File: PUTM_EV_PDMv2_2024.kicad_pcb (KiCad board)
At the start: 4 copper layers, 58 x 87.3 mm, 138 parts, among them IC1 BTS722204ESAXUMA1, IC2 BTS722204ESAXUMA1, IC3 BTS722204ESAXUMA1, IC4 BTS722204ESAXUMA1, J1 74650073R, J4 Conn_01x06, J5 UMPT-08-01-L-RA-WT-P-TR, J6 FTSH-107-01-L-DV-K-A, J7 USB_C_Receptacle_USB2.0_14P, J8 UMPT-08-01-L-RA-WT-P-TR, U1 STM32G0C1KCTxN, U2 LD1117S33TR_SOT223, U3 LM2675M-5.0/NOPB, U4 MCP2542FDxMF

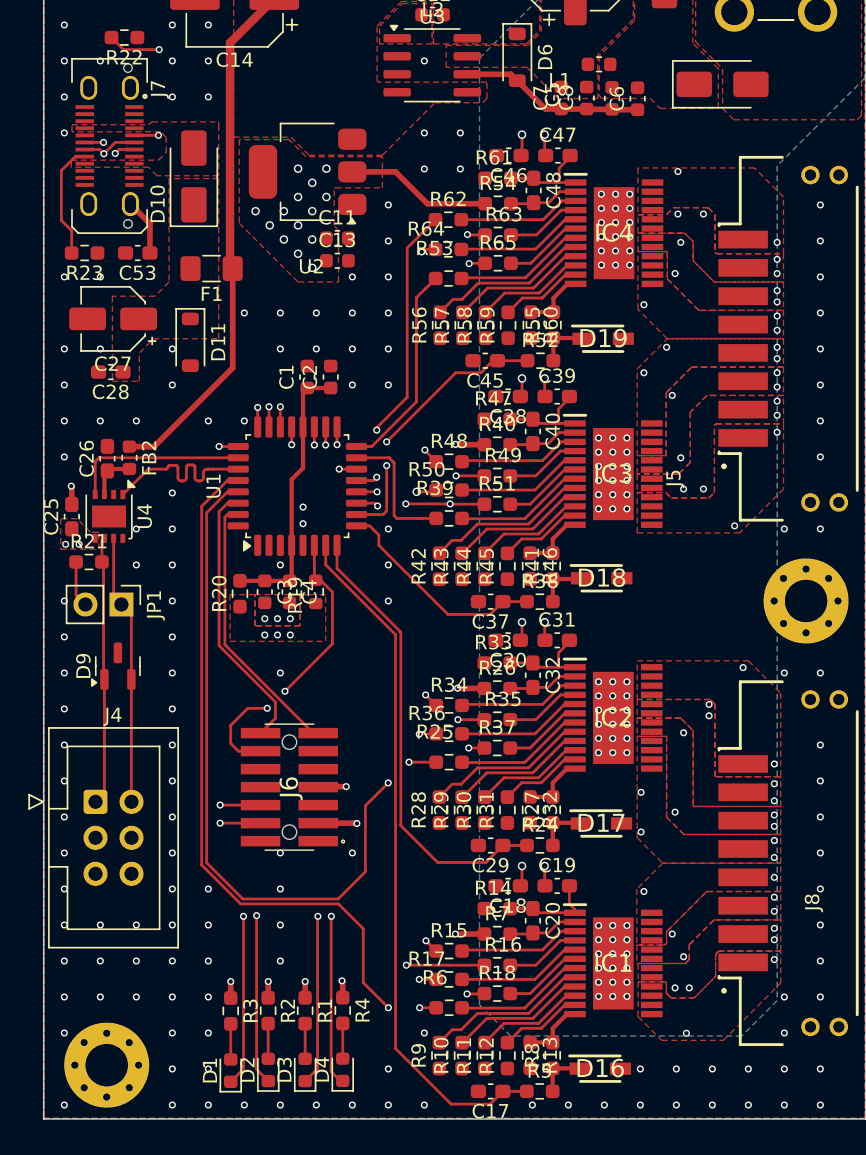
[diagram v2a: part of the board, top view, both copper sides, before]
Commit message: Minor changes
Added battery zone on the f.cu
Easier connector soldering (additional pads)
Changed 3.3V layer
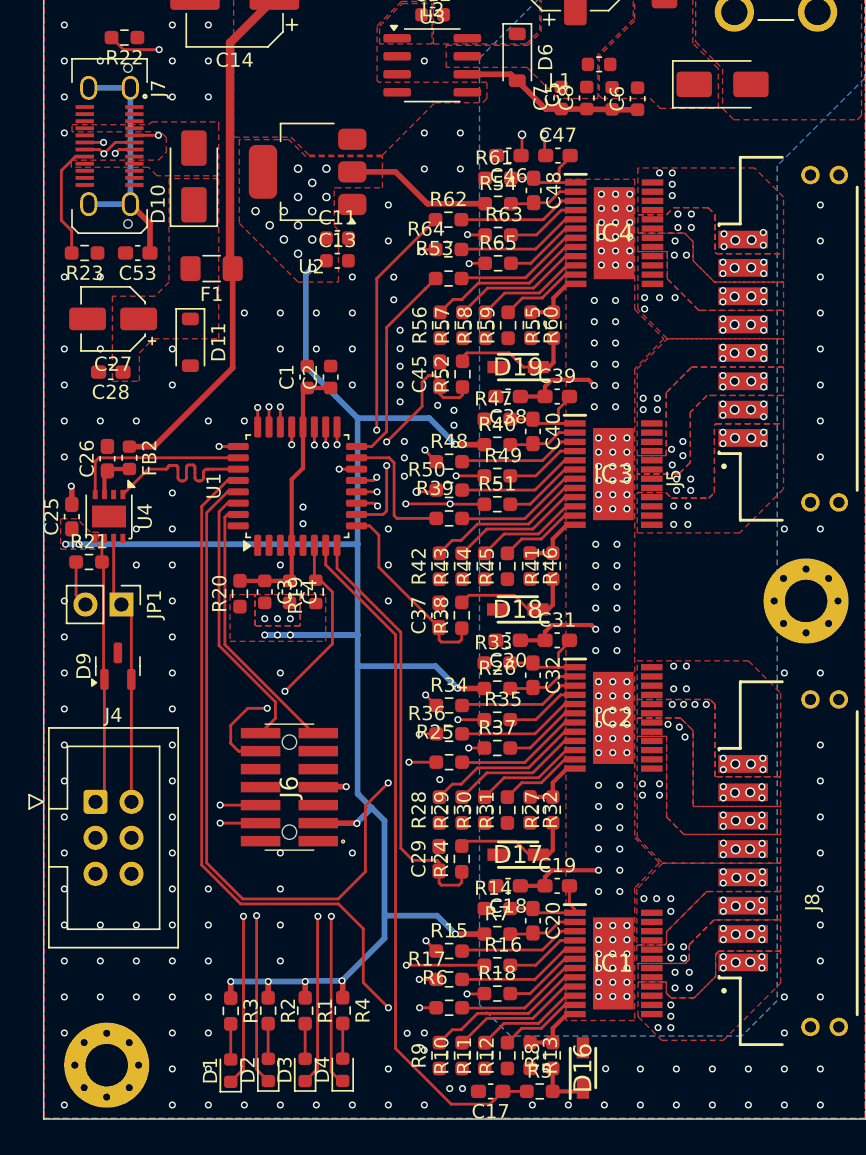
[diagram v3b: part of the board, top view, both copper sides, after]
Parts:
- moved D19 6.32 mm to (154.3, 88.8), turned to 180 degrees
- moved D18 6.32 mm to (154.2, 105.8), turned to 180 degrees
- moved D17 6.27 mm to (154.3, 123.2), turned to 180 degrees
- moved R38 5.60 mm to (150.3, 106.3), turned to 90 degrees
- moved R24 5.59 mm to (150.3, 123.5), turned to 90 degrees
- moved R52 5.58 mm to (150.3, 89.2), turned to 90 degrees
- moved C37 3.76 mm to (148.7, 106.3), turned to 90 degrees
- moved C29 3.76 mm to (148.7, 123.4), turned to 90 degrees
- moved C45 3.35 mm to (148.8, 89.2), turned to 90 degrees
- moved D16 1.23 mm to (158.8, 138.2), turned to 90 degrees
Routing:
- net +BATT: track 11.1 -> 21.9 mm, vias 80 -> 110
- net Net-(D19-K): track 3.70 -> 9.11 mm
- net Net-(D17-K): track 3.63 -> 9.02 mm
- net Net-(D18-K): track 3.65 -> 9.00 mm
- net /FUSE4_IS: track 19.4 -> 17.2 mm
- net /FUSE3_IS: track 15.4 -> 13.5 mm
- net /FUSE2_IS: track 32.1 -> 30.3 mm
- net OUT4_3: vias 3 -> 10
- net OUT4_2: vias 4 -> 9
- net OUT4_1: vias 4 -> 10
- net OUT4_0: vias 2 -> 10
- net OUT3_3: vias 2 -> 10
- net OUT3_2: vias 4 -> 10
- net OUT3_1: vias 4 -> 10
- net OUT3_0: vias 4 -> 10
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- added copper zone on B.Cu, net OUT1_0
- added copper zone on B.Cu, net OUT1_1
- added copper zone on B.Cu, net OUT1_2
- added copper zone on B.Cu, net OUT1_3
- added copper zone on B.Cu, net OUT2_0
- added copper zone on B.Cu, net OUT2_1
- added copper zone on B.Cu, net OUT2_2
- added copper zone on B.Cu, net OUT2_3
- added copper zone on B.Cu, net OUT3_0
- added copper zone on B.Cu, net OUT3_1
- added copper zone on B.Cu, net OUT3_2
- added copper zone on B.Cu, net OUT3_3
- added copper zone on B.Cu, net OUT4_0
- added copper zone on B.Cu, net OUT4_1
- added copper zone on B.Cu, net OUT4_2
- added copper zone on B.Cu, net OUT4_3

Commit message: Production
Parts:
- added C21: 10n, Capacitor_SMD:C_0603_1608Metric_Pad1.08x0.95mm_HandSolder, B.Cu at (173.2, 124.8)
- added C22: 10n, Capacitor_SMD:C_0603_1608Metric_Pad1.08x0.95mm_HandSolder, B.Cu at (173.2, 126.8)
- added C23: 10n, Capacitor_SMD:C_0603_1608Metric_Pad1.08x0.95mm_HandSolder, B.Cu at (173.2, 128.8)
- added C24: 10n, Capacitor_SMD:C_0603_1608Metric_Pad1.08x0.95mm_HandSolder, B.Cu at (173.2, 130.8)
- added C33: 10n, Capacitor_SMD:C_0603_1608Metric_Pad1.08x0.95mm_HandSolder, B.Cu at (173.2, 116.8)
- added C34: 10n, Capacitor_SMD:C_0603_1608Metric_Pad1.08x0.95mm_HandSolder, B.Cu at (173.2, 118.8)
- added C35: 10n, Capacitor_SMD:C_0603_1608Metric_Pad1.08x0.95mm_HandSolder, B.Cu at (173.2, 120.8)
- added C36: 10n, Capacitor_SMD:C_0603_1608Metric_Pad1.08x0.95mm_HandSolder, B.Cu at (173.2, 122.8)
- added C41: 10n, Capacitor_SMD:C_0603_1608Metric_Pad1.08x0.95mm_HandSolder, B.Cu at (173.3, 87.7)
- added C42: 10n, Capacitor_SMD:C_0603_1608Metric_Pad1.08x0.95mm_HandSolder, B.Cu at (173.3, 89.7)
- added C43: 10n, Capacitor_SMD:C_0603_1608Metric_Pad1.08x0.95mm_HandSolder, B.Cu at (173.3, 91.8)
- added C44: 10n, Capacitor_SMD:C_0603_1608Metric_Pad1.08x0.95mm_HandSolder, B.Cu at (173.2, 93.8)
- added C49: 10n, Capacitor_SMD:C_0603_1608Metric_Pad1.08x0.95mm_HandSolder, B.Cu at (173.3, 79.8)
- added C50: 10n, Capacitor_SMD:C_0603_1608Metric_Pad1.08x0.95mm_HandSolder, B.Cu at (173.3, 81.8)
- added C51: 10n, Capacitor_SMD:C_0603_1608Metric_Pad1.08x0.95mm_HandSolder, B.Cu at (173.3, 83.8)
- added C52: 10n, Capacitor_SMD:C_0603_1608Metric_Pad1.08x0.95mm_HandSolder, B.Cu at (173.3, 85.8)
- added G***: LOGO, LOGO, F.Cu at (127.5, 88.3)
- added G***: LOGO, LOGO, B.Cu at (165.8, 104.8)
- added G***: LOGO, Logos:SignatureBox25mm, B.Cu at (153.7, 60.6)
- added G***: LOGO, LOGO, B.Cu at (175.5, 139.0)
- added G***: LOGO, logos:PUTM_LOGO_15mm, B.Cu at (135.7, 58.3)
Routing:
- net OUT4_0: track 0.00 -> 1.09 mm
- net OUT2_1: track 0.00 -> 1.07 mm
- net OUT2_2: track 0.00 -> 1.04 mm
- net OUT2_3: track 0.00 -> 1.03 mm
- net OUT1_3: track 0.00 -> 1.03 mm
- net OUT4_3: track 0.00 -> 1.02 mm
- net OUT4_2: track 0.00 -> 1.02 mm
- net OUT4_1: track 0.00 -> 1.02 mm
- net OUT1_2: track 0.00 -> 0.99 mm
- net OUT1_1: track 0.00 -> 0.99 mm
- net OUT3_2: track 0.00 -> 0.98 mm
- net OUT2_0: track 0.00 -> 0.97 mm
- net OUT3_1: track 0.00 -> 0.96 mm
- net OUT3_0: track 0.00 -> 0.96 mm
- net OUT3_3: track 0.00 -> 0.95 mm
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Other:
- board text added: "Kacper Biadała"
- board text added: "v2.0"

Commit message: Production
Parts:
- removed the G*** at (127.5, 88.3)

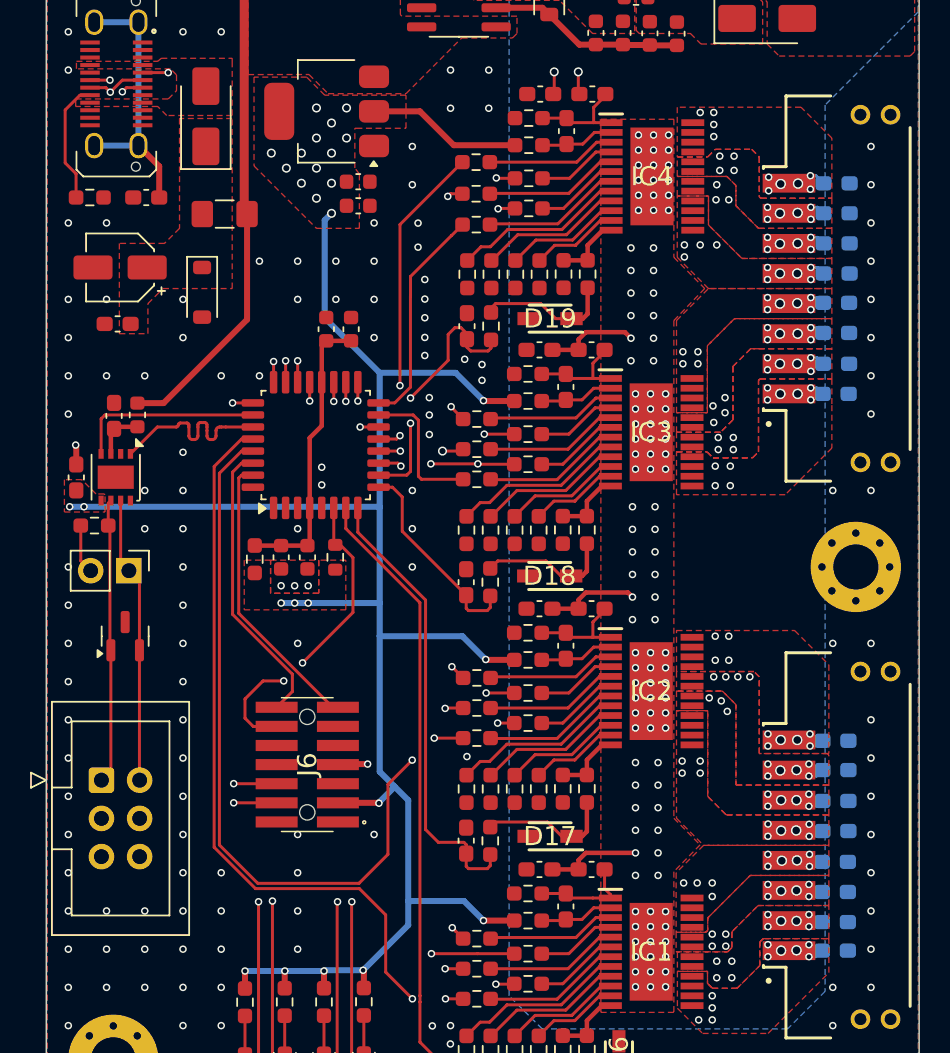
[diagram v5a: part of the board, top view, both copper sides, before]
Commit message: Minor fixes
added USBc tvs
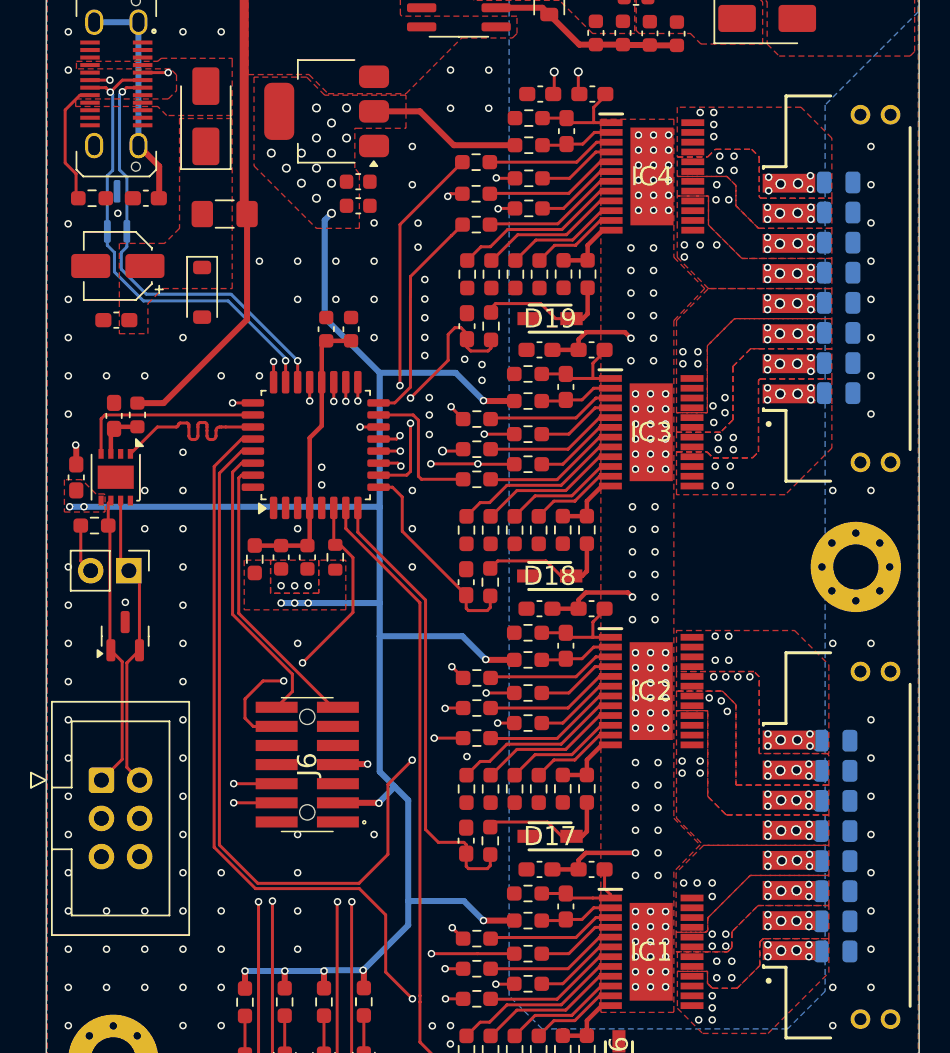
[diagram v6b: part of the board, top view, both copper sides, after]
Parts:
- added D12: TPD2E2U06QDCKRQ1, Package_TO_SOT_SMD:SOT-323_SC-70_Handsoldering, B.Cu at (125.5, 81.6)
- C21, C22, C23, C24, C33, C34, C35, C36, C41, C42, C43, C44, C49, C50, C51, C52: footprint Capacitor_SMD:C_0603_1608Metric_Pad1.08x0.95mm_HandSolder -> Capacitor_SMD:C_0805_2012Metric
- moved C28 0.26 mm to (125.5, 88.8)
- moved C44 0.21 mm to (173.4, 93.7)
- moved C27 0.18 mm to (125.5, 85.2)
- moved C43 0.18 mm to (173.4, 91.7)
- moved C41 0.17 mm to (173.4, 87.7)
- moved C42 0.17 mm to (173.4, 89.7)
- moved R23 0.16 mm to (123.8, 80.8)
- moved C49 0.15 mm to (173.4, 79.7)
- moved C50 0.15 mm to (173.4, 81.7)
- moved C51 0.15 mm to (173.4, 83.7)
- moved C52 0.15 mm to (173.4, 85.7)
- moved C24 0.07 mm to (173.2, 130.8)
- moved C21 0.07 mm to (173.2, 124.8)
- moved C22 0.07 mm to (173.2, 126.8)
- moved C23 0.07 mm to (173.2, 128.8)
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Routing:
- net /D-: track 28.2 -> 31.8 mm
- net /D+: track 28.2 -> 31.7 mm
- net OUT4_0: track 1.09 -> 0.00 mm
- net OUT2_1: track 1.07 -> 0.00 mm
- net OUT2_2: track 1.04 -> 0.00 mm
- net OUT2_3: track 1.03 -> 0.00 mm
- net OUT1_3: track 1.03 -> 0.00 mm
- net OUT4_3: track 1.02 -> 0.00 mm
- net OUT4_2: track 1.02 -> 0.00 mm
- net OUT4_1: track 1.02 -> 0.00 mm
- net OUT1_2: track 0.99 -> 0.00 mm
- net OUT1_1: track 0.99 -> 0.00 mm
- net OUT3_2: track 0.98 -> 0.00 mm
- net OUT2_0: track 0.97 -> 0.00 mm
- net OUT3_1: track 0.96 -> 0.00 mm
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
